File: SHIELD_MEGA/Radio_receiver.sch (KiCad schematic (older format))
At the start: 6 parts

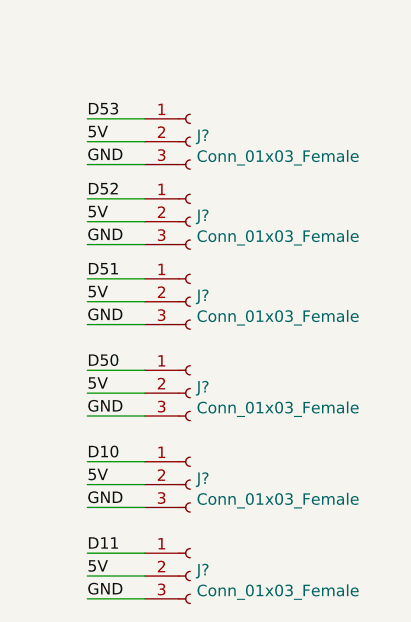
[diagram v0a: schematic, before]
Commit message: Changing conections on receiver sheet
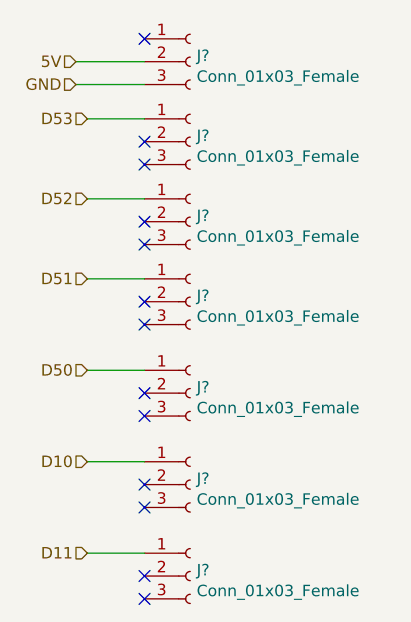
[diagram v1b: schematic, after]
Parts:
- added J?: Conn_01x03_Female, symbol Connector:Conn_01x03_Female
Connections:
- net 5V: now also J?.2 (Pin_2); no longer J?.2 (Pin_2), J?.2 (Pin_2), J?.2 (Pin_2), J?.2 (Pin_2), J?.2 (Pin_2), J?.2 (Pin_2)
- net GND: now also J?.3 (Pin_3); no longer J?.3 (Pin_3), J?.3 (Pin_3), J?.3 (Pin_3), J?.3 (Pin_3), J?.3 (Pin_3), J?.3 (Pin_3)
- no-connect marks 0 -> 13
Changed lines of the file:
@@
 $Descr A4 11693 8268
 encoding utf-8
-Sheet 5 9
+Sheet 9 10
 Title ""
 Date ""
@@
 	1    0    0    -1
 $EndComp
-Text Label 5300 5050 0    50   ~ 0
-GND
-Wire Wire Line
-	5300 5050 5550 5050
-Text Label 5300 4950 0    50   ~ 0
-5V
-Wire Wire Line
-	5300 4950 5550 4950
-Text Label 5300 4850 0    50   ~ 0
-D11
-Wire Wire Line
-	5300 4850 5550 4850
-Text Label 5300 4650 0    50   ~ 0
-GND
-Wire Wire Line
-	5300 4650 5550 4650
-Wire Wire Line
-	5550 4550 5300 4550
-Text Label 5300 4550 0    50   ~ 0
-5V
-Text Label 5300 4450 0    50   ~ 0
-D10
 Wire Wire Line
 	5300 4450 5550 4450
 Wire Wire Line
-	5550 4250 5300 4250
-Text Label 5300 4250 0    50   ~ 0
-GND
-Text Label 5300 4150 0    50   ~ 0
-5V
-Wire Wire Line
-	5300 4150 5550 4150
-Wire Wire Line
 	5550 4050 5300 4050
-Text Label 5300 4050 0    50   ~ 0
-D50
-Text Label 5300 3850 0    50   ~ 0
-GND
-Wire Wire Line
-	5300 3850 5550 3850
-Wire Wire Line
-	5550 3750 5300 3750
-Text Label 5300 3750 0    50   ~ 0
-5V
-Text Label 5300 3650 0    50   ~ 0
-D51
 Wire Wire Line
 	5300 3650 5550 3650
 Wire Wire Line
-	5550 3500 5300 3500
-Text Label 5300 3500 0    50   ~ 0
-GND
-Text Label 5300 3400 0    50   ~ 0
+	5550 3300 5300 3300
+Wire Wire Line
+	5300 2950 5550 2950
+Text HLabel 5300 2950 0    50   Input ~ 0
+D53
+Text HLabel 5300 3300 0    50   Input ~ 0
+D52
+Text HLabel 5300 3650 0    50   Input ~ 0
+D51
+Text HLabel 5300 4050 0    50   Input ~ 0
+D50
+Text HLabel 5300 4450 0    50   Input ~ 0
+D10
+Text HLabel 5300 4850 0    50   Input ~ 0
+D11
+$Comp
+L Connector:Conn_01x03_Female J?
+U 1 1 61B78C5D
+P 5750 2700
+F 0 "J?" H 5778 2726 50  0000 L CNN
+F 1 "Conn_01x03_Female" H 5778 2635 50  0000 L CNN
+F 2 "" H 5750 2700 50  0001 C CNN
+F 3 "~" H 5750 2700 50  0001 C CNN
+	1    5750 2700
+	1    0    0    -1
+$EndComp
+Text HLabel 5250 2700 0    50   Input ~ 0
 5V
 Wire Wire Line
-	5300 3400 5550 3400
+	5250 2700 5550 2700
 Wire Wire Line
-	5550 3300 5300 3300
-Text Label 5300 3300 0    50   ~ 0
-D52
+	5550 2800 5250 2800
+Text HLabel 5250 2800 0    50   Input ~ 0
+GND
+NoConn ~ 5550 2600
+NoConn ~ 5550 3050
+NoConn ~ 5550 3150
+NoConn ~ 5550 3400
+NoConn ~ 5550 3500
+NoConn ~ 5550 3750
+NoConn ~ 5550 3850
+NoConn ~ 5550 4150
+NoConn ~ 5550 4250
 Wire Wire Line
-	5550 3150 5300 3150
-Text Label 5300 3150 0    50   ~ 0
-GND
-Wire Wire Line
-	5300 3050 5550 3050
-Text Label 5300 3050 0    50   ~ 0
-5V
-Wire Wire Line
-	5300 2950 5550 2950
-Text Label 5300 2950 0    50   ~ 0
-D53
+	5300 4850 5550 4850
+NoConn ~ 5550 4950
+NoConn ~ 5550 5050
+NoConn ~ 5550 4650
+NoConn ~ 5550 4550
 $EndSCHEMATC

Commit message: Anotations of ref. parts in radio receptor sheet
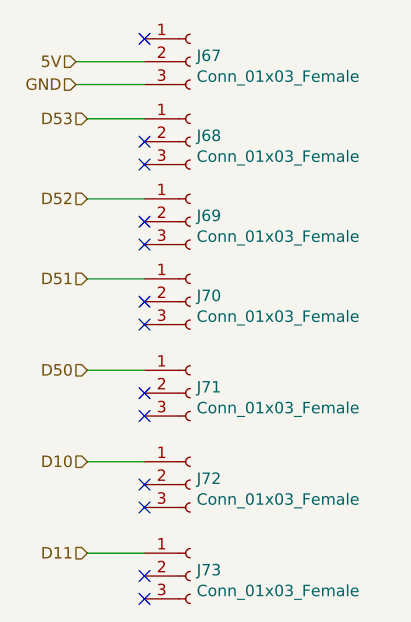
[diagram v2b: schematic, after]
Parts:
- gave numbers to parts that had none: 7
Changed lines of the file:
@@
 encoding utf-8
 Sheet 9 10
-Title ""
-Date ""
-Rev ""
-Comp ""
+Title "SHIELD ARDUINO MEGA"
+Date "2021-11-21"
+Rev "V1"
+Comp "PROEX - UNIFEI"
 Comment1 ""
 Comment2 ""
 Comment3 ""
-Comment4 ""
+Comment4 "LINCOLN WALLACE VELOSO ALMEIDA"
 $EndDescr
 $Comp
-L Connector:Conn_01x03_Female J?
+L Connector:Conn_01x03_Female J68
 U 1 1 61973E8C
 P 5750 3050
-F 0 "J?" H 5778 3076 50  0000 L CNN
+F 0 "J68" H 5778 3076 50  0000 L CNN
 F 1 "Conn_01x03_Female" H 5778 2985 50  0000 L CNN
 F 2 "" H 5750 3050 50  0001 C CNN
@@
 $EndComp
 $Comp
-L Connector:Conn_01x03_Female J?
+L Connector:Conn_01x03_Female J69
 U 1 1 61974EE4
 P 5750 3400
-F 0 "J?" H 5778 3426 50  0000 L CNN
+F 0 "J69" H 5778 3426 50  0000 L CNN
 F 1 "Conn_01x03_Female" H 5778 3335 50  0000 L CNN
 F 2 "" H 5750 3400 50  0001 C CNN
@@
 $EndComp
 $Comp
-L Connector:Conn_01x03_Female J?
+L Connector:Conn_01x03_Female J70
 U 1 1 6197586F
 P 5750 3750
-F 0 "J?" H 5778 3776 50  0000 L CNN
+F 0 "J70" H 5778 3776 50  0000 L CNN
 F 1 "Conn_01x03_Female" H 5778 3685 50  0000 L CNN
 F 2 "" H 5750 3750 50  0001 C CNN
@@
 $EndComp
 $Comp
-L Connector:Conn_01x03_Female J?
+L Connector:Conn_01x03_Female J71
 U 1 1 61975F3B
 P 5750 4150
-F 0 "J?" H 5778 4176 50  0000 L CNN
+F 0 "J71" H 5778 4176 50  0000 L CNN
 F 1 "Conn_01x03_Female" H 5778 4085 50  0000 L CNN
 F 2 "" H 5750 4150 50  0001 C CNN
@@
 $EndComp
 $Comp
-L Connector:Conn_01x03_Female J?
+L Connector:Conn_01x03_Female J72
 U 1 1 61976273
 P 5750 4550
-F 0 "J?" H 5778 4576 50  0000 L CNN
+F 0 "J72" H 5778 4576 50  0000 L CNN
 F 1 "Conn_01x03_Female" H 5778 4485 50  0000 L CNN
 F 2 "" H 5750 4550 50  0001 C CNN
@@
 $EndComp
 $Comp
-L Connector:Conn_01x03_Female J?
+L Connector:Conn_01x03_Female J73
 U 1 1 61976608
 P 5750 4950
-F 0 "J?" H 5778 4976 50  0000 L CNN
+F 0 "J73" H 5778 4976 50  0000 L CNN
 F 1 "Conn_01x03_Female" H 5778 4885 50  0000 L CNN
 F 2 "" H 5750 4950 50  0001 C CNN
@@
 D11
 $Comp
-L Connector:Conn_01x03_Female J?
+L Connector:Conn_01x03_Female J67
 U 1 1 61B78C5D
 P 5750 2700
-F 0 "J?" H 5778 2726 50  0000 L CNN
+F 0 "J67" H 5778 2726 50  0000 L CNN
 F 1 "Conn_01x03_Female" H 5778 2635 50  0000 L CNN
 F 2 "" H 5750 2700 50  0001 C CNN
